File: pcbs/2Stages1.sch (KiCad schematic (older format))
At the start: 13 parts, among them Q1 MBT3904DW1, Q2 MBT3904DW1, U2 LM324QT

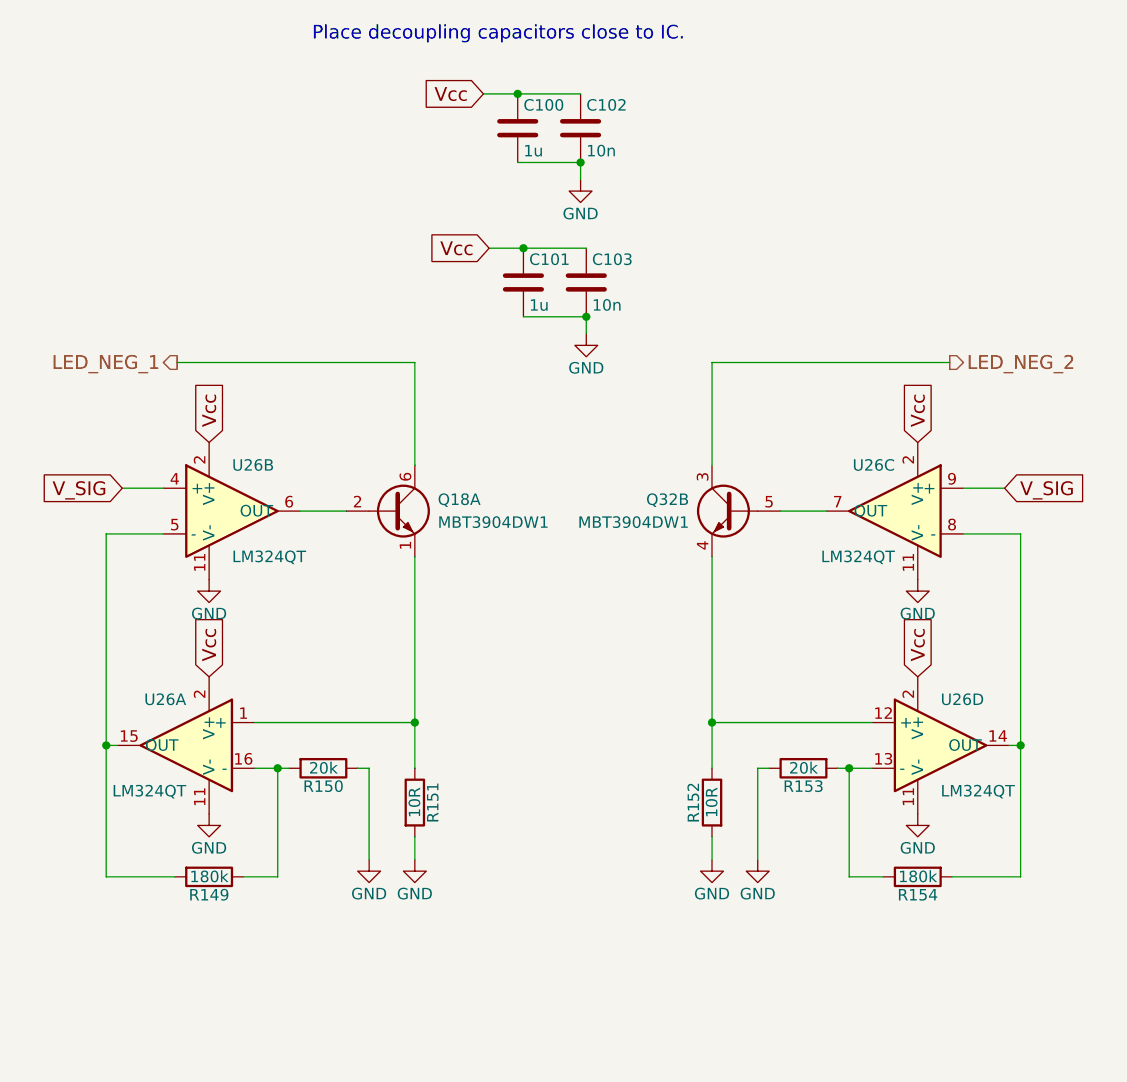
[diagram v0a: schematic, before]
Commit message: Only UI is left for schematics.
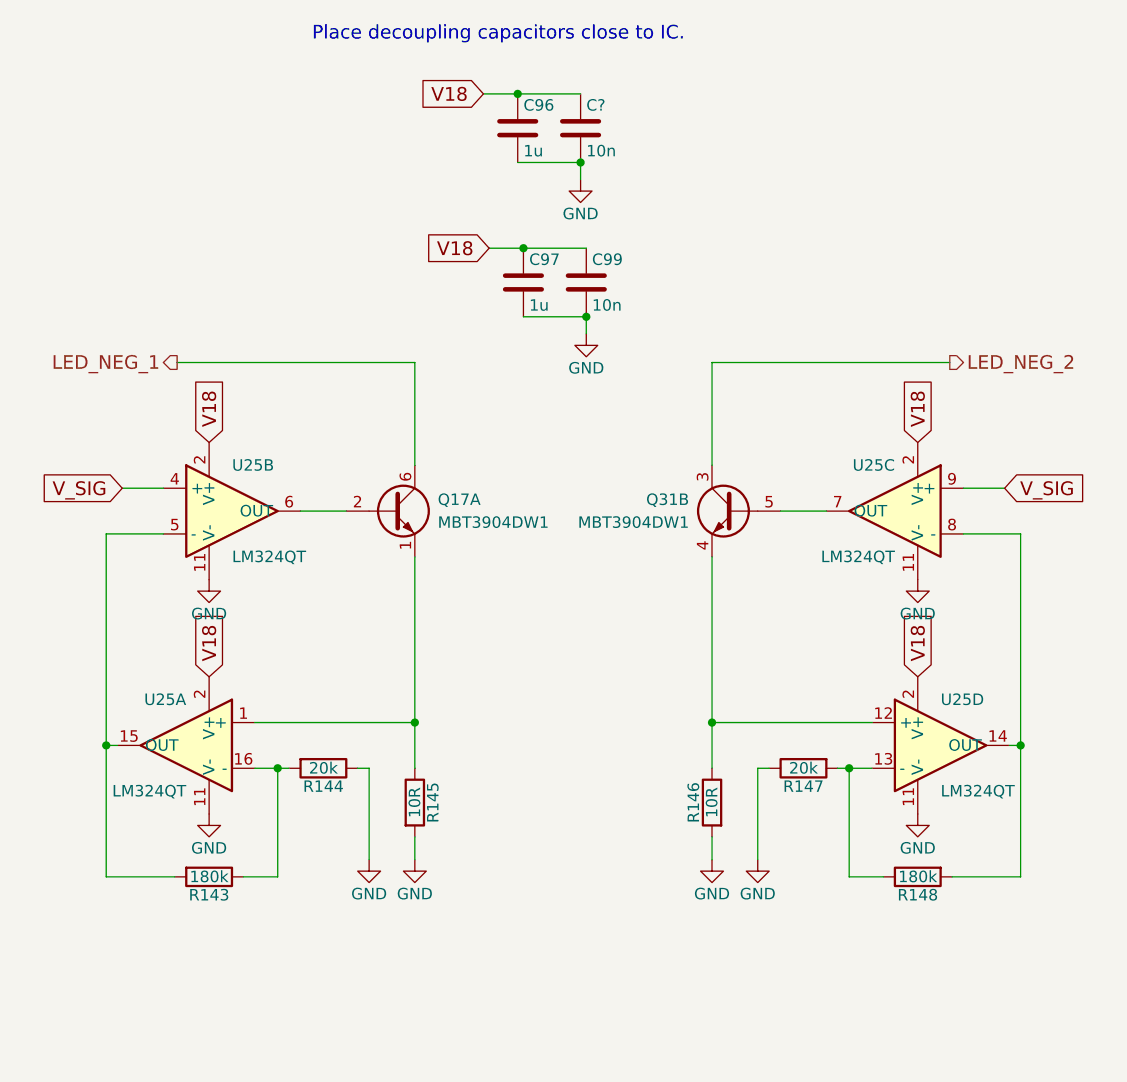
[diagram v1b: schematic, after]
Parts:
- removed C6: 10n, Resistors_SMD:R_0603, symbol C
- added C?: 10n, Resistors_SMD:R_0603, symbol C
- C7: Digikey 490-7194-1-ND -> 311-1085-1-ND
- U2: footprint QFN:QFN-16-1EP_3x3mm_Pitch0.5mm_ThermalVias -> QFN:QFN-16-1EP_3x3mm_Pitch0.5mm
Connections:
- net GND: now also C?.2
- net Vcc renamed V18
- net V18: now also C?.1

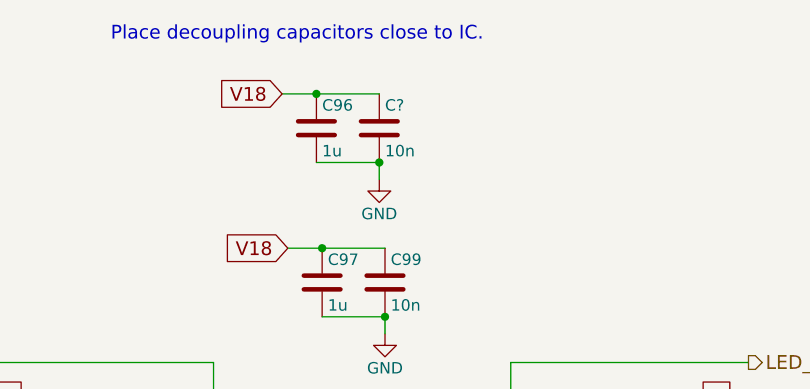
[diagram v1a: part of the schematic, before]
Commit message: Almost done with schematics. SPI OLED is missing.
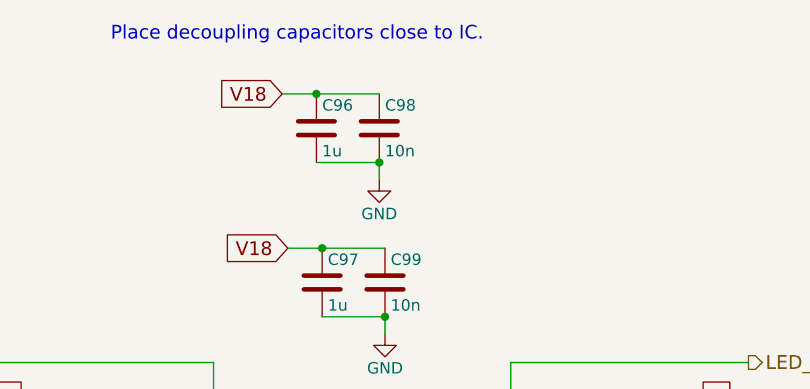
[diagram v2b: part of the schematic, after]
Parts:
- gave numbers to parts that had none: 1
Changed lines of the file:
@@
 LIBS:mydacs
 LIBS:mydcdcs
+LIBS:switches
+LIBS:mytactilesw
 LIBS:led_driver-cache
 EELAYER 25 0
@@
 AR Path="/5A0916C5/5A09BEC0/5A1597B5" Ref="U22"  Part="2"
 AR Path="/5A0916C5/5A09BEC4/5A1597B5" Ref="U23"  Part="2"
-AR Path="/5A0916C5/5A09BEC8/5A1597B5" Ref="U24"  Part="1"
+AR Path="/5A0916C5/5A09BEC8/5A1597B5" Ref="U24"  Part="2"
 AR Path="/5A0916C5/5A09BECC/5A1597B5" Ref="U25"  Part="2"
 AR Path="/5A0916C5/5A09BED0/5A1597B5" Ref="U26"  Part="2"
@@
 AR Path="/5A0916C5/5A09BEC0/5A1597BC" Ref="U22"  Part="1"
 AR Path="/5A0916C5/5A09BEC4/5A1597BC" Ref="U23"  Part="1"
-AR Path="/5A0916C5/5A09BEC8/5A1597BC" Ref="U24"  Part="2"
+AR Path="/5A0916C5/5A09BEC8/5A1597BC" Ref="U24"  Part="1"
 AR Path="/5A0916C5/5A09BECC/5A1597BC" Ref="U25"  Part="1"
 AR Path="/5A0916C5/5A09BED0/5A1597BC" Ref="U26"  Part="1"
@@
 	4150 3350 3970 3350
 $Comp
-L C C?
+L C C6
 U 1 1 5A0B232F
 P 5975 1775
-AR Path="/5A0916C5/5A09BEC4/5A0B232F" Ref="C?"  Part="1"
-AR Path="/5A0916C5/5A09BEC8/5A0B232F" Ref="C?"  Part="1"
-AR Path="/5A0916C5/5A09BED0/5A0B232F" Ref="C?"  Part="1"
-AR Path="/5A0916C5/5A09BECC/5A0B232F" Ref="C?"  Part="1"
-F 0 "C?" H 6000 1875 50  0000 L CNN
+AR Path="/5A0916C5/5A0A220F/5A0B232F" Ref="C6"  Part="1"
+AR Path="/5A0916C5/5A096F49/5A0B232F" Ref="C10"  Part="1"
+AR Path="/5A0916C5/5A0972CC/5A0B232F" Ref="C14"  Part="1"
+AR Path="/5A0916C5/5A0972D0/5A0B232F" Ref="C18"  Part="1"
+AR Path="/5A0916C5/5A097A65/5A0B232F" Ref="C22"  Part="1"
+AR Path="/5A0916C5/5A097A69/5A0B232F" Ref="C26"  Part="1"
+AR Path="/5A0916C5/5A097A6D/5A0B232F" Ref="C30"  Part="1"
+AR Path="/5A0916C5/5A097A71/5A0B232F" Ref="C34"  Part="1"
+AR Path="/5A0916C5/5A0988AE/5A0B232F" Ref="C38"  Part="1"
+AR Path="/5A0916C5/5A0988B2/5A0B232F" Ref="C42"  Part="1"
+AR Path="/5A0916C5/5A0988B6/5A0B232F" Ref="C46"  Part="1"
+AR Path="/5A0916C5/5A0988BA/5A0B232F" Ref="C50"  Part="1"
+AR Path="/5A0916C5/5A0988BE/5A0B232F" Ref="C54"  Part="1"
+AR Path="/5A0916C5/5A0988C2/5A0B232F" Ref="C58"  Part="1"
+AR Path="/5A0916C5/5A0988C6/5A0B232F" Ref="C62"  Part="1"
+AR Path="/5A0916C5/5A0988CA/5A0B232F" Ref="C66"  Part="1"
+AR Path="/5A0916C5/5A09BEB0/5A0B232F" Ref="C70"  Part="1"
+AR Path="/5A0916C5/5A09BEB4/5A0B232F" Ref="C74"  Part="1"
+AR Path="/5A0916C5/5A09BEB8/5A0B232F" Ref="C78"  Part="1"
+AR Path="/5A0916C5/5A09BEBC/5A0B232F" Ref="C82"  Part="1"
+AR Path="/5A0916C5/5A09BEC0/5A0B232F" Ref="C86"  Part="1"
+AR Path="/5A0916C5/5A09BEC4/5A0B232F" Ref="C90"  Part="1"
+AR Path="/5A0916C5/5A09BEC8/5A0B232F" Ref="C94"  Part="1"
+AR Path="/5A0916C5/5A09BECC/5A0B232F" Ref="C98"  Part="1"
+AR Path="/5A0916C5/5A09BED0/5A0B232F" Ref="C102"  Part="1"
+AR Path="/5A0916C5/5A09BED4/5A0B232F" Ref="C106"  Part="1"
+AR Path="/5A0916C5/5A09BED8/5A0B232F" Ref="C110"  Part="1"
+AR Path="/5A0916C5/5A09BEDC/5A0B232F" Ref="C114"  Part="1"
+AR Path="/5A0916C5/5A09BEE0/5A0B232F" Ref="C118"  Part="1"
+AR Path="/5A0916C5/5A09BEE4/5A0B232F" Ref="C122"  Part="1"
+AR Path="/5A0916C5/5A09BEE8/5A0B232F" Ref="C126"  Part="1"
+AR Path="/5A0916C5/5A09BEEC/5A0B232F" Ref="C130"  Part="1"
+F 0 "C98" H 6000 1875 50  0000 L CNN
 F 1 "10n" H 6000 1675 50  0000 L CNN
 F 2 "Resistors_SMD:R_0603" H 6013 1625 50  0001 C CNN

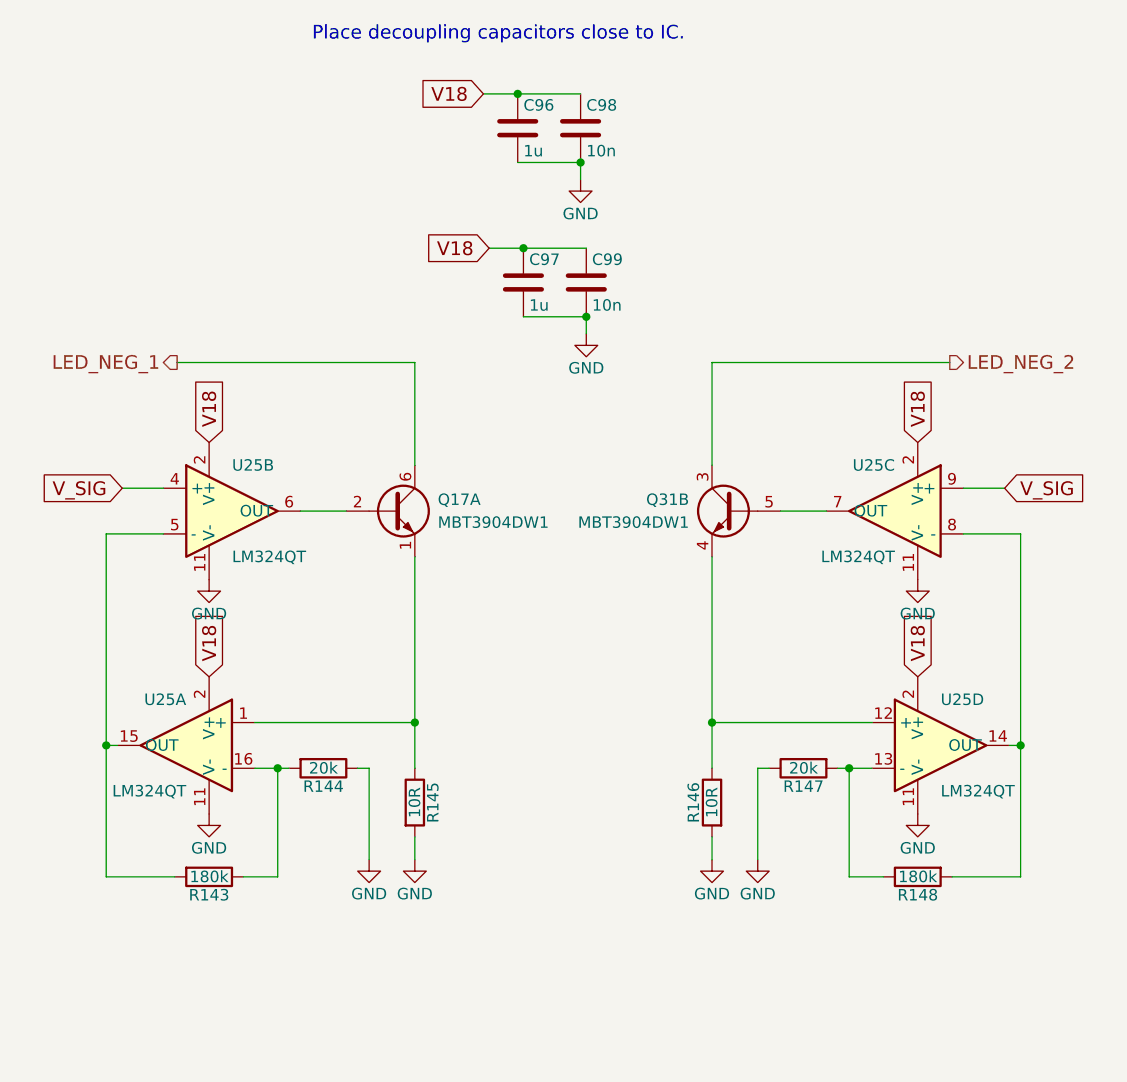
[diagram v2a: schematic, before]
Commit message: No DRC errors anymore in schematics.
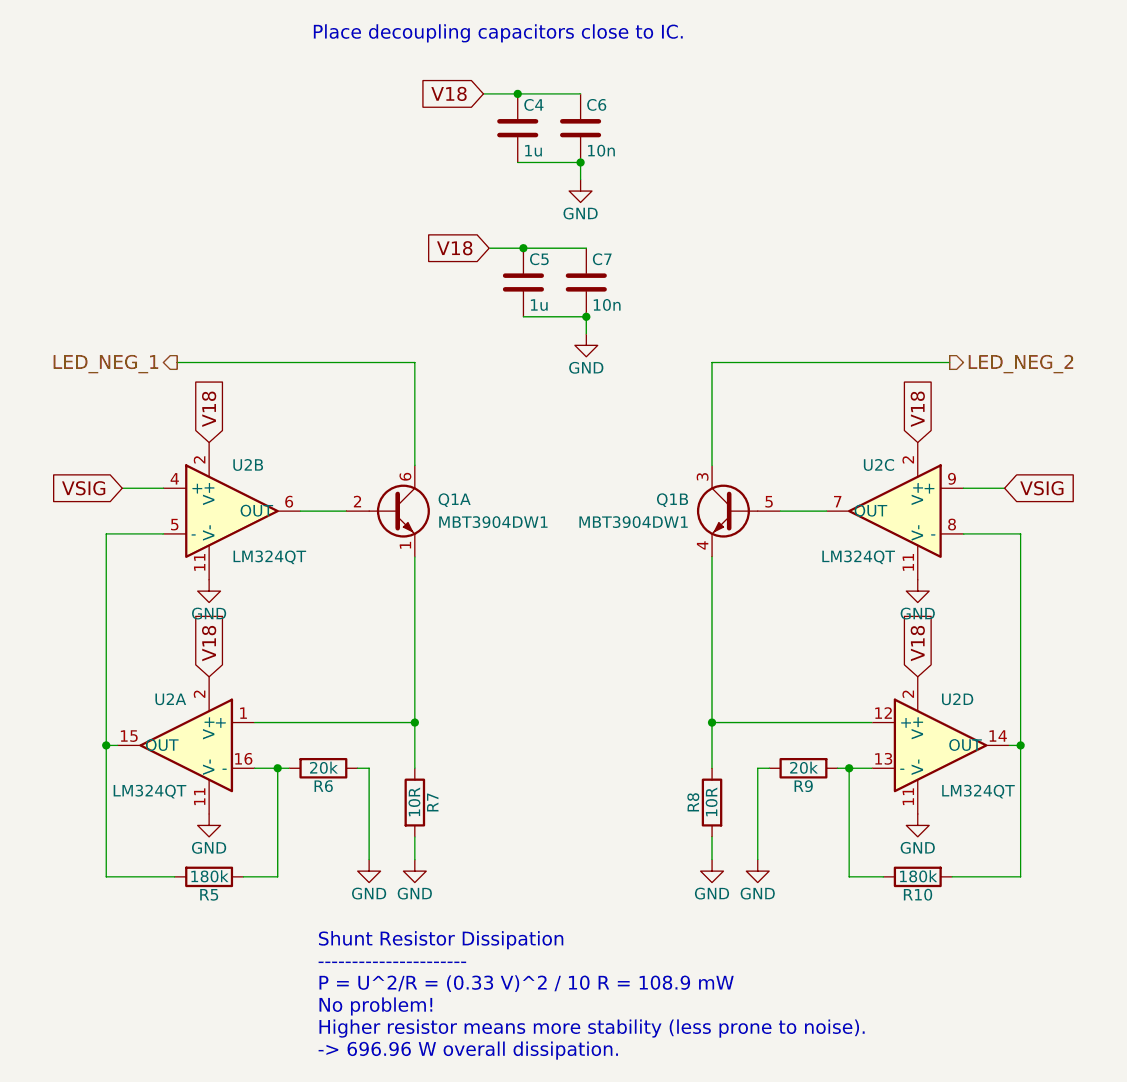
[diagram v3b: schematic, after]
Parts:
- renumbered Q2 to Q1
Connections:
- net V_SIG renamed VSIG
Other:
- note added: "Shunt Resistor Dissipation\n----------------------\nP = U^2/R = (0.33 V)^2 / 10 R = 108.9 mW\nNo problem!\nHigher resistor means more stability (less prone to noise).\n-> 696.96 W overall dissipation."
